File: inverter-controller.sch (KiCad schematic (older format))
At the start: 0 parts

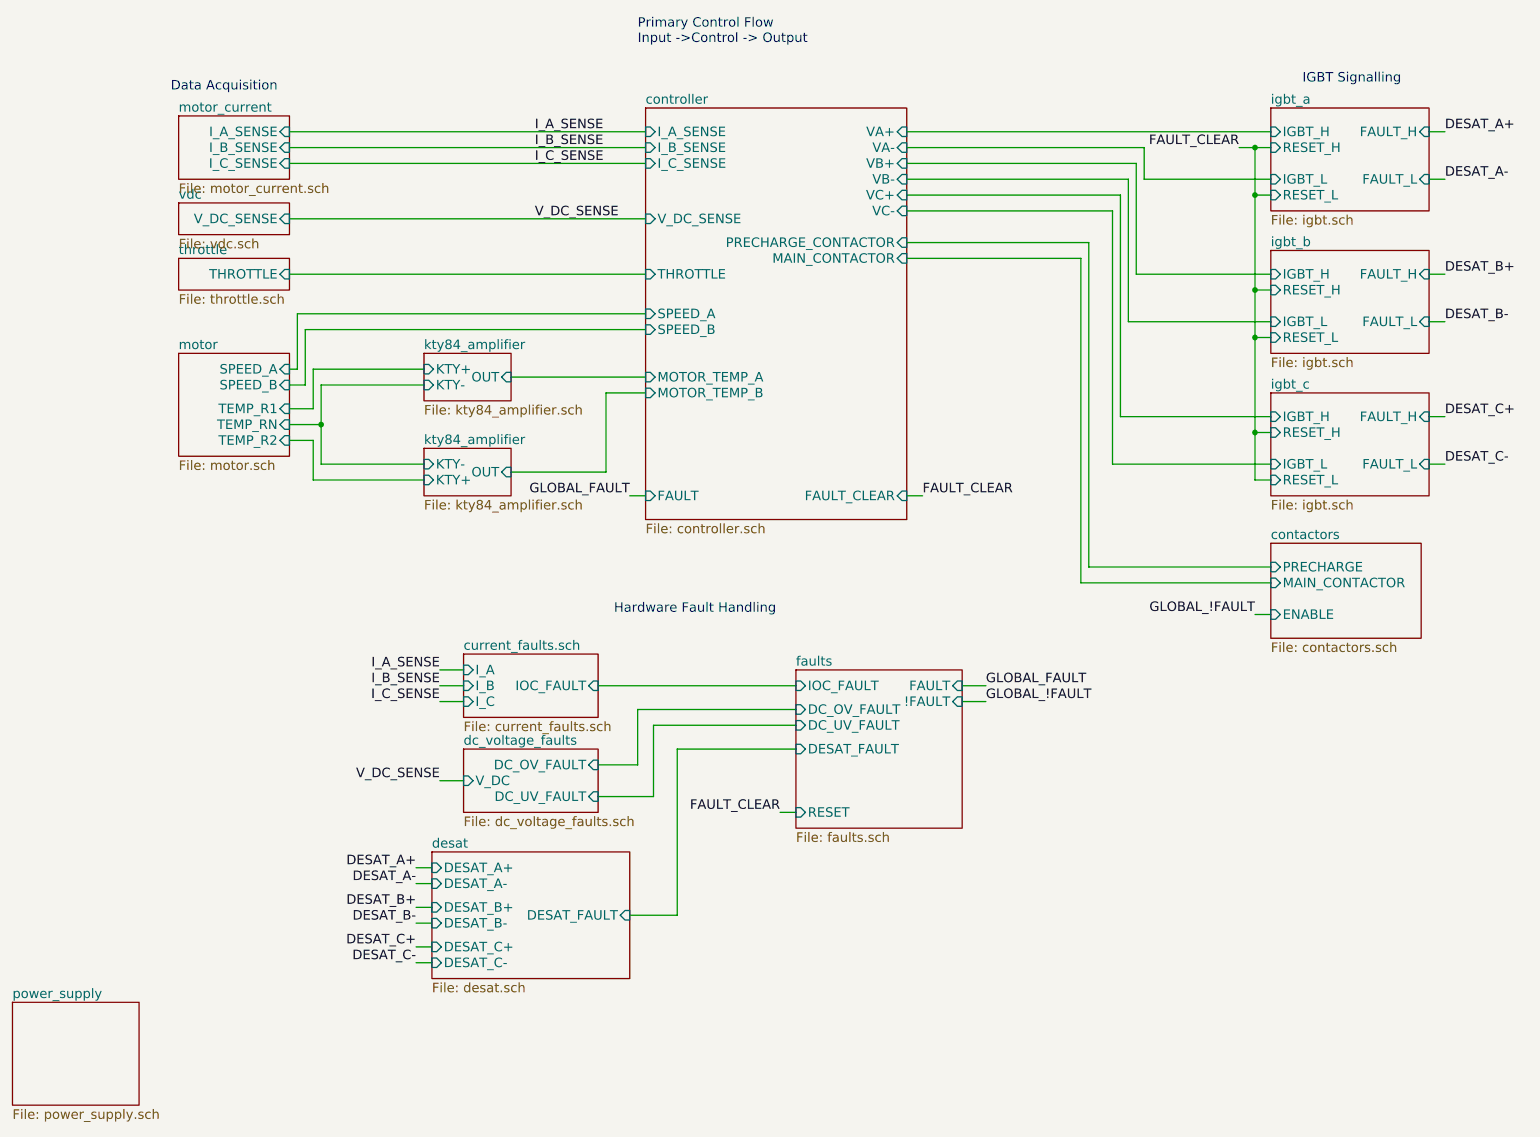
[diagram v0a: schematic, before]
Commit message: Adds IOC reference points.
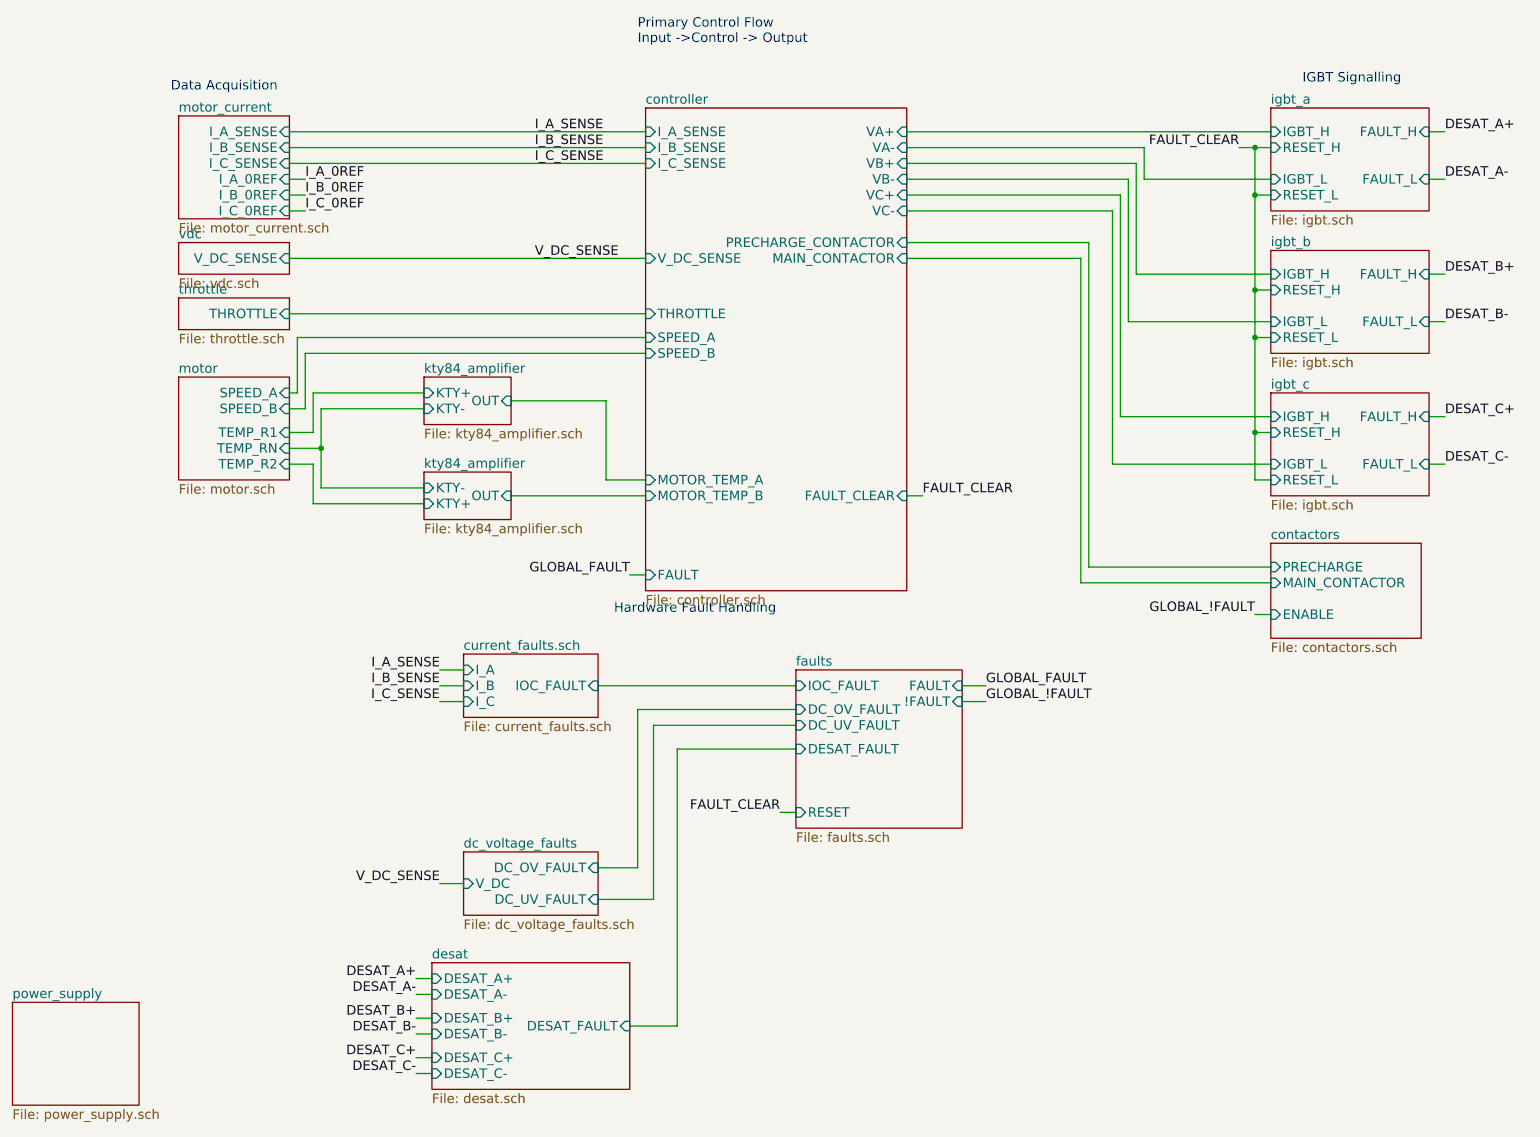
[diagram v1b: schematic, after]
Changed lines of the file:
@@
 $EndDescr
 $Sheet
-S 4850 1150 1650 2600
+S 4850 1150 1650 3050
 U 5AEC1F05
 F0 "controller" 60
@@
 F9 "I_B_SENSE" I L 4850 1400 60
 F10 "I_C_SENSE" I L 4850 1500 60
-F11 "V_DC_SENSE" I L 4850 1850 60
-F12 "THROTTLE" I L 4850 2200 60
-F13 "FAULT" I L 4850 3600 60
+F11 "V_DC_SENSE" I L 4850 2100 60
+F12 "THROTTLE" I L 4850 2450 60
+F13 "FAULT" I L 4850 4100 60
 F14 "FAULT_CLEAR" I R 6500 3600 60
-F15 "SPEED_A" I L 4850 2450 60
-F16 "SPEED_B" I L 4850 2550 60
-F17 "MOTOR_TEMP_A" I L 4850 2850 60
-F18 "MOTOR_TEMP_B" I L 4850 2950 60
+F15 "SPEED_A" I L 4850 2600 60
+F16 "SPEED_B" I L 4850 2700 60
+F17 "MOTOR_TEMP_A" I L 4850 3500 60
+F18 "MOTOR_TEMP_B" I L 4850 3600 60
 F19 "PRECHARGE_CONTACTOR" I R 6500 2000 60
 F20 "MAIN_CONTACTOR" I R 6500 2100 60
@@
 $EndSheet
 $Sheet
-S 1900 2700 700  650
+S 1900 2850 700  650
 U 5AEDE197
 F0 "motor" 60
 F1 "motor.sch" 60
-F2 "SPEED_A" I R 2600 2800 60
-F3 "SPEED_B" I R 2600 2900 60
-F4 "TEMP_R1" I R 2600 3050 60
-F5 "TEMP_R2" I R 2600 3250 60
-F6 "TEMP_RN" I R 2600 3150 60
-$EndSheet
-$Sheet
-S 1900 1200 700  400
-U 5AEC7636
-F0 "motor_current" 60
-F1 "motor_current.sch" 60
-F2 "I_A_SENSE" I R 2600 1300 60
-F3 "I_B_SENSE" I R 2600 1400 60
-F4 "I_C_SENSE" I R 2600 1500 60
-$EndSheet
-$Sheet
-S 1900 2100 700  200
+F2 "SPEED_A" I R 2600 2950 60
+F3 "SPEED_B" I R 2600 3050 60
+F4 "TEMP_R1" I R 2600 3200 60
+F5 "TEMP_R2" I R 2600 3400 60
+F6 "TEMP_RN" I R 2600 3300 60
+$EndSheet
+$Sheet
+S 1900 2350 700  200
 U 5AEE00A3
 F0 "throttle" 60
 F1 "throttle.sch" 60
-F2 "THROTTLE" I R 2600 2200 60
-$EndSheet
-$Sheet
-S 1900 1750 700  200
+F2 "THROTTLE" I R 2600 2450 60
+$EndSheet
+$Sheet
+S 1900 2000 700  200
 U 5AEE7A72
 F0 "vdc" 60
 F1 "vdc.sch" 60
-F2 "V_DC_SENSE" I R 2600 1850 60
+F2 "V_DC_SENSE" I R 2600 2100 60
 $EndSheet
 Wire Wire Line
@@
 	7850 3100 8800 3100
 Wire Wire Line
-	4850 1850 2600 1850
+	4850 2100 2600 2100
 Wire Wire Line
 	8000 1400 8000 1600
@@
 	7800 3400 8800 3400
 Wire Wire Line
-	2600 2200 4850 2200
+	2600 2450 4850 2450
 Wire Wire Line
 	6500 1400 8000 1400
@@
 	6500 1600 7900 1600
 $Sheet
-S 3500 5850 1250 800
+S 3500 6550 1250 800
 U 5AF0A5AE
 F0 "desat" 60
 F1 "desat.sch" 60
-F2 "DESAT_A+" I L 3500 5950 60
-F3 "DESAT_A-" I L 3500 6050 60
-F4 "DESAT_B+" I L 3500 6200 60
-F5 "DESAT_B-" I L 3500 6300 60
-F6 "DESAT_C+" I L 3500 6450 60
-F7 "DESAT_C-" I L 3500 6550 60
-F8 "DESAT_FAULT" I R 4750 6250 60
+F2 "DESAT_A+" I L 3500 6650 60
+F3 "DESAT_A-" I L 3500 6750 60
+F4 "DESAT_B+" I L 3500 6900 60
+F5 "DESAT_B-" I L 3500 7000 60
+F6 "DESAT_C+" I L 3500 7150 60
+F7 "DESAT_C-" I L 3500 7250 60
+F8 "DESAT_FAULT" I R 4750 6950 60
 $EndSheet
 Text Label 4150 1300 0    60   ~ 0
@@
 	4550 4800 5800 4800
 Wire Wire Line
-	5050 6250 5050 5200
+	5050 6950 5050 5200
 Wire Wire Line
 	5050 5200 5800 5200
 Wire Wire Line
-	4750 6250 5050 6250
+	4750 6950 5050 6950
 Wire Wire Line
 	5700 5600 5800 5600
@@
 Text Label 6600 3600 0    60   ~ 0
 FAULT_CLEAR
-Text Label 4750 3600 2    60   ~ 0
+Text Label 4750 4100 2    60   ~ 0
 GLOBAL_FAULT
 Wire Wire Line
-	4750 3600 4850 3600
+	4750 4100 4850 4100
 Wire Wire Line
 	6600 3600 6500 3600
 $Sheet
-S 3450 2700 550  300
+S 3450 2850 550  300
 U 5AF6F00C
 F0 "kty84_amplifier" 60
 F1 "kty84_amplifier.sch" 60
-F2 "KTY+" I L 3450 2800 60
-F3 "KTY-" I L 3450 2900 60
-F4 "OUT" I R 4000 2850 60
-$EndSheet
-$Sheet
-S 3450 3300 550  300
+F2 "KTY+" I L 3450 2950 60
+F3 "KTY-" I L 3450 3050 60
+F4 "OUT" I R 4000 3000 60
+$EndSheet
+$Sheet
+S 3450 3450 550  300
 U 5AF71A27
 F0 "kty84_amplifier" 60
 F1 "kty84_amplifier.sch" 60
-F2 "KTY+" I L 3450 3500 60
-F3 "KTY-" I L 3450 3400 60
-F4 "OUT" I R 4000 3450 60
-$EndSheet
-Wire Wire Line
-	2600 3150 2800 3150
-Wire Wire Line
-	2800 2900 2800 3400
-Wire Wire Line
-	2800 2900 3450 2900
-Wire Wire Line
-	2800 3400 3450 3400
-Connection ~ 2800 3150
-Wire Wire Line
-	2600 3050 2750 3050
-Wire Wire Line
-	2750 3050 2750 2800
-Wire Wire Line
-	2750 2800 3450 2800
-Wire Wire Line
-	2600 3250 2750 3250
-Wire Wire Line
-	2750 3250 2750 3500
-Wire Wire Line
-	2750 3500 3450 3500
-Wire Wire Line
-	2600 2900 2700 2900
-Wire Wire Line
-	2700 2900 2700 2550
-Wire Wire Line
-	2700 2550 4850 2550
-Wire Wire Line
-	2650 2800 2600 2800
-Wire Wire Line
-	2650 2450 2650 2800
-Wire Wire Line
-	2650 2450 4850 2450
-Wire Wire Line
-	4000 2850 4850 2850
-Wire Wire Line
-	4000 3450 4600 3450
-Wire Wire Line
-	4600 3450 4600 2950
-Wire Wire Line
-	4600 2950 4850 2950
+F2 "KTY+" I L 3450 3650 60
+F3 "KTY-" I L 3450 3550 60
+F4 "OUT" I R 4000 3600 60
+$EndSheet
+Wire Wire Line
+	2600 3300 2800 3300
+Wire Wire Line
+	2800 3050 2800 3300
+Wire Wire Line
+	2800 3300 2800 3550
+Wire Wire Line
+	2800 3050 3450 3050
+Wire Wire Line
+	2800 3550 3450 3550
+Connection ~ 2800 3300
+Wire Wire Line
+	2600 3200 2750 3200
+Wire Wire Line
+	2750 3200 2750 2950
+Wire Wire Line
+	2750 2950 3450 2950
+Wire Wire Line
+	2600 3400 2750 3400
+Wire Wire Line
+	2750 3400 2750 3650
+Wire Wire Line
+	2750 3650 3450 3650
+Wire Wire Line
+	2600 3050 2700 3050
+Wire Wire Line
+	2700 3050 2700 2700
+Wire Wire Line
+	2700 2700 4850 2700
+Wire Wire Line
+	2650 2950 2600 2950
+Wire Wire Line
+	2650 2600 2650 2950
+Wire Wire Line
+	2650 2600 4850 2600
+Wire Wire Line
+	4000 3600 4850 3600
 Text Label 9900 1300 0    60   ~ 0
 DESAT_A+
@@
 Wire Wire Line
 	9900 3400 9800 3400
-Text Label 4150 1850 0    60   ~ 0
+Text Label 4150 2100 0    60   ~ 0
 V_DC_SENSE
 $Sheet
-S 3700 5200 850  400
+S 3700 5850 850  400
 U 5AF92467
 F0 "dc_voltage_faults" 60
 F1 "dc_voltage_faults.sch" 60
-F2 "V_DC" I L 3700 5400 60
-F3 "DC_OV_FAULT" I R 4550 5300 60
-F4 "DC_UV_FAULT" I R 4550 5500 60
-$EndSheet
-Wire Wire Line
-	4550 5300 4800 5300
-Wire Wire Line
-	4800 5300 4800 4950
+F2 "V_DC" I L 3700 6050 60
+F3 "DC_OV_FAULT" I R 4550 5950 60
+F4 "DC_UV_FAULT" I R 4550 6150 60
+$EndSheet
+Wire Wire Line
+	4550 5950 4800 5950
+Wire Wire Line
+	4800 5950 4800 4950
 Wire Wire Line
 	4800 4950 5800 4950
@@
 	5800 5050 4900 5050
 Wire Wire Line
-	4900 5050 4900 5500
-Wire Wire Line
-	4900 5500 4550 5500
-Text Label 3550 5400 2    60   ~ 0
+	4900 5050 4900 6150
+Wire Wire Line
+	4900 6150 4550 6150
+Text Label 3550 6050 2    60   ~ 0
 V_DC_SENSE
 Wire Wire Line
-	3550 5400 3700 5400
-Text Label 3400 5950 2    60   ~ 0
+	3550 6050 3700 6050
+Text Label 3400 6650 2    60   ~ 0
 DESAT_A+
-Text Label 3400 6050 2    60   ~ 0
+Text Label 3400 6750 2    60   ~ 0
 DESAT_A-
-Text Label 3400 6200 2    60   ~ 0
+Text Label 3400 6900 2    60   ~ 0
 DESAT_B+
-Text Label 3400 6300 2    60   ~ 0
+Text Label 3400 7000 2    60   ~ 0
 DESAT_B-
-Text Label 3400 6450 2    60   ~ 0
+Text Label 3400 7150 2    60   ~ 0
 DESAT_C+
-Text Label 3400 6550 2    60   ~ 0
+Text Label 3400 7250 2    60   ~ 0
 DESAT_C-
 Wire Wire Line
-	3400 5950 3500 5950
-Wire Wire Line
-	3400 6050 3500 6050
-Wire Wire Line
-	3400 6200 3500 6200
-Wire Wire Line
-	3400 6300 3500 6300
-Wire Wire Line
-	3400 6450 3500 6450
-Wire Wire Line
-	3400 6550 3500 6550
+	3400 6650 3500 6650
+Wire Wire Line
+	3400 6750 3500 6750
+Wire Wire Line
+	3400 6900 3500 6900
+Wire Wire Line
+	3400 7000 3500 7000
+Wire Wire Line
+	3400 7150 3500 7150
+Wire Wire Line
+	3400 7250 3500 7250
 Text Label 8600 1400 2    60   ~ 0
 FAULT_CLEAR
 Wire Wire Line
-	8600 1400 8800 1400
-Wire Wire Line
-	8700 1400 8700 3500
+	8600 1400 8700 1400
+Wire Wire Line
+	8700 1400 8800 1400
+Wire Wire Line
+	8700 1400 8700 1700
+Wire Wire Line
+	8700 1700 8700 2300
+Wire Wire Line
+	8700 2300 8700 2600
+Wire Wire Line
+	8700 2600 8700 3200
+Wire Wire Line
+	8700 3200 8700 3500
 Wire Wire Line
 	8700 3500 8800 3500
@@
 Wire Wire Line
 	8700 4350 8800 4350
+Wire Wire Line
+	4000 3000 4600 3000
+Wire Wire Line
+	4600 3000 4600 3500
+Wire Wire Line
+	4600 3500 4850 3500
+$Sheet
+S 1900 1200 700  650
+U 5AEC7636
+F0 "motor_current" 60
+F1 "motor_current.sch" 60
+F2 "I_A_SENSE" I R 2600 1300 60
+F3 "I_B_SENSE" I R 2600 1400 60
+F4 "I_C_SENSE" I R 2600 1500 60
+F5 "I_A_0REF" I R 2600 1600 60
+F6 "I_B_0REF" I R 2600 1700 60
+F7 "I_C_0REF" I R 2600 1800 60
+$EndSheet
+Text Label 2700 1600 0    60   ~ 0
+I_A_0REF
+Text Label 2700 1700 0    60   ~ 0
+I_B_0REF
+Text Label 2700 1800 0    60   ~ 0
+I_C_0REF
+Wire Wire Line
+	2600 1600 2700 1600
+Wire Wire Line
+	2600 1700 2700 1700
+Wire Wire Line
+	2600 1800 2700 1800
 $EndSCHEMATC
